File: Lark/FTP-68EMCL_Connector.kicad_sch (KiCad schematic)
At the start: 6 parts, among them J3 B34B-PHDSS

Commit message: added power section to schematic
It needs revised, due to thermal issue. Specifically in regards to my soft start circuit, the mosfet wont be able to handle the power dissipated during a slow turn on.
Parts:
- C16: value 0.1 µF -> 0.1µF
- C17: value 6800 µF -> 6800µF
- D7: footprint onsemi:D_SOD-523 -> onsemi:ESD5Z3.3T1G
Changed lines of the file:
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@@
 			)
 		)
-		(property "Datasheet" "https://www.seielect.com/catalog/SEI-RMCF_RMCP.pdf"
+		(property "Datasheet" "~"
 			(at 49.53 128.27 0)
 			(effects
@@
 			)
 		)
-		(property "Value" "0.1 µF"
+		(property "Value" "0.1µF"
 			(at 38.1 137.1662 0)
 			(effects
@@
 			)
 		)
-		(property "Datasheet" "https://search.murata.co.jp/Ceramy/image/img/A01X/G101/ENG/GRM188R72A104MA35-01A.pdf"
+		(property "Datasheet" "~"
 			(at 35.56 135.89 0)
 			(effects
@@
 			)
 		)
-		(property "Datasheet" "https://www.seielect.com/catalog/SEI-RMCF_RMCP.pdf"
+		(property "Datasheet" "~"
 			(at 35.56 119.38 0)
 			(effects
@@
 			)
 		)
-		(property "Value" "6800 µF"
+		(property "Value" "6800µF"
 			(at 92.71 128.6509 0)
 			(effects
@@
 			)
 		)
-		(property "Footprint" "onsemi:D_SOD-523"
+		(property "Footprint" "onsemi:ESD5Z3.3T1G"
 			(at 57.15 137.16 0)
 			(effects

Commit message: update, WIP
- Reannotated schematic.
- Added STM32 device.
- Fixed High-side switch (removed soft-start cap for device safety).
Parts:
- renumbered C17 to C26, C16 to C27, D7 to D9, J3 to J4, R34 to R41, R33 to R42
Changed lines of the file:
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@@
 		(on_board yes)
 		(dnp no)
-		(property "Reference" "R33"
+		(property "Reference" "R42"
 			(at 50.546 125.73 90)
 			(effects
@@
 			(project "Lark"
 				(path "/a351af57-4353-47da-9f45-7393de572768/6e291d34-e508-4d3b-a2e9-20acfef2b928"
-					(reference "R33")
+					(reference "R42")
 					(unit 1)
 				)
@@
 		(dnp no)
 		(fields_autoplaced yes)
-		(property "Reference" "#PWR069"
+		(property "Reference" "#PWR0109"
 			(at 226.06 33.02 0)
 			(effects
@@
 			(project "Lark"
 				(path "/a351af57-4353-47da-9f45-7393de572768/6e291d34-e508-4d3b-a2e9-20acfef2b928"
-					(reference "#PWR069")
+					(reference "#PWR0109")
 					(unit 1)
 				)
@@
 		(on_board yes)
 		(dnp no)
-		(property "Reference" "C16"
+		(property "Reference" "C27"
 			(at 38.1 134.6262 0)
 			(effects
@@
 			(project "Lark"
 				(path "/a351af57-4353-47da-9f45-7393de572768/6e291d34-e508-4d3b-a2e9-20acfef2b928"
-					(reference "C16")
+					(reference "C27")
 					(unit 1)
 				)
@@
 		(dnp no)
 		(fields_autoplaced yes)
-		(property "Reference" "#PWR088"
+		(property "Reference" "#PWR0110"
 			(at 251.46 33.02 0)
 			(effects
@@
 			(project "Lark"
 				(path "/a351af57-4353-47da-9f45-7393de572768/6e291d34-e508-4d3b-a2e9-20acfef2b928"
-					(reference "#PWR088")
+					(reference "#PWR0110")
 					(unit 1)
 				)
@@
 		(on_board yes)
 		(dnp no)
-		(property "Reference" "R34"
+		(property "Reference" "R41"
 			(at 38.1 118.1099 0)
 			(effects
@@
 			(project "Lark"
 				(path "/a351af57-4353-47da-9f45-7393de572768/6e291d34-e508-4d3b-a2e9-20acfef2b928"
-					(reference "R34")
+					(reference "R41")
 					(unit 1)
 				)
@@
 		(dnp no)
 		(fields_autoplaced yes)
-		(property "Reference" "#PWR090"
+		(property "Reference" "#PWR0114"
 			(at 248.92 95.25 0)
 			(effects
@@
 			(project "Lark"
 				(path "/a351af57-4353-47da-9f45-7393de572768/6e291d34-e508-4d3b-a2e9-20acfef2b928"
-					(reference "#PWR090")
+					(reference "#PWR0114")
 					(unit 1)
 				)
@@
 		(dnp no)
 		(fields_autoplaced yes)
-		(property "Reference" "#PWR071"
+		(property "Reference" "#PWR0113"
 			(at 228.6 95.25 0)
 			(effects
@@
 			(project "Lark"
 				(path "/a351af57-4353-47da-9f45-7393de572768/6e291d34-e508-4d3b-a2e9-20acfef2b928"
-					(reference "#PWR071")
+					(reference "#PWR0113")
 					(unit 1)
 				)
@@
 		(dnp no)
 		(fields_autoplaced yes)
-		(property "Reference" "#PWR091"
+		(property "Reference" "#PWR0116"
 			(at 88.9 115.57 0)
 			(effects
@@
 			(project "Lark"
 				(path "/a351af57-4353-47da-9f45-7393de572768/6e291d34-e508-4d3b-a2e9-20acfef2b928"
-					(reference "#PWR091")
+					(reference "#PWR0116")
 					(unit 1)
 				)
@@
 		(dnp no)
 		(fields_autoplaced yes)
-		(property "Reference" "#PWR070"
+		(property "Reference" "#PWR0111"
 			(at 220.98 39.37 0)
 			(effects
@@
 			(project "Lark"
 				(path "/a351af57-4353-47da-9f45-7393de572768/6e291d34-e508-4d3b-a2e9-20acfef2b928"
-					(reference "#PWR070")
+					(reference "#PWR0111")
 					(unit 1)
 				)
@@
 		(dnp no)
 		(fields_autoplaced yes)
-		(property "Reference" "#PWR086"
+		(property "Reference" "#PWR0115"
 			(at 35.56 115.57 0)
 			(effects
@@
 			(project "Lark"
 				(path "/a351af57-4353-47da-9f45-7393de572768/6e291d34-e508-4d3b-a2e9-20acfef2b928"
-					(reference "#PWR086")
+					(reference "#PWR0115")
 					(unit 1)
 				)
@@
 		(dnp no)
 		(fields_autoplaced yes)
-		(property "Reference" "C17"
+		(property "Reference" "C26"
 			(at 92.71 126.1109 0)
 			(effects
@@
 			(project ""
 				(path "/a351af57-4353-47da-9f45-7393de572768/6e291d34-e508-4d3b-a2e9-20acfef2b928"
-					(reference "C17")
+					(reference "C26")
 					(unit 1)
 				)
@@
 		(dnp no)
 		(fields_autoplaced yes)
-		(property "Reference" "D7"
+		(property "Reference" "D9"
 			(at 59.69 136.6201 90)
 			(effects
@@
 			(project "Lark"
 				(path "/a351af57-4353-47da-9f45-7393de572768/6e291d34-e508-4d3b-a2e9-20acfef2b928"
-					(reference "D7")
+					(reference "D9")
 					(unit 1)
 				)
@@
 		(dnp no)
 		(fields_autoplaced yes)
-		(property "Reference" "#PWR089"
+		(property "Reference" "#PWR0112"
 			(at 256.54 39.37 0)
 			(effects
@@
 			(project "Lark"
 				(path "/a351af57-4353-47da-9f45-7393de572768/6e291d34-e508-4d3b-a2e9-20acfef2b928"
-					(reference "#PWR089")
+					(reference "#PWR0112")
 					(unit 1)
 				)
@@
 		(on_board yes)
 		(dnp no)
-		(property "Reference" "J3"
+		(property "Reference" "J4"
 			(at 236.982 37.592 0)
 			(effects
@@
 			(project ""
 				(path "/a351af57-4353-47da-9f45-7393de572768/6e291d34-e508-4d3b-a2e9-20acfef2b928"
-					(reference "J3")
+					(reference "J4")
 					(unit 1)
 				)
@@
 		(dnp no)
 		(fields_autoplaced yes)
-		(property "Reference" "#PWR085"
+		(property "Reference" "#PWR0118"
 			(at 57.15 151.13 0)
 			(effects
@@
 			(project "Lark"
 				(path "/a351af57-4353-47da-9f45-7393de572768/6e291d34-e508-4d3b-a2e9-20acfef2b928"
-					(reference "#PWR085")
+					(reference "#PWR0118")
 					(unit 1)
 				)
@@
 		(dnp no)
 		(fields_autoplaced yes)
-		(property "Reference" "#PWR087"
+		(property "Reference" "#PWR0117"
 			(at 35.56 151.13 0)
 			(effects
@@
 			(project "Lark"
 				(path "/a351af57-4353-47da-9f45-7393de572768/6e291d34-e508-4d3b-a2e9-20acfef2b928"
-					(reference "#PWR087")
+					(reference "#PWR0117")
 					(unit 1)
 				)
@@
 		(dnp no)
 		(fields_autoplaced yes)
-		(property "Reference" "#PWR092"
+		(property "Reference" "#PWR0119"
 			(at 88.9 151.13 0)
 			(effects
@@
 			(project "Lark"
 				(path "/a351af57-4353-47da-9f45-7393de572768/6e291d34-e508-4d3b-a2e9-20acfef2b928"
-					(reference "#PWR092")
-					(unit 1)
-				)
+					(reference "#PWR0119")
+					(unit 1)
+				)

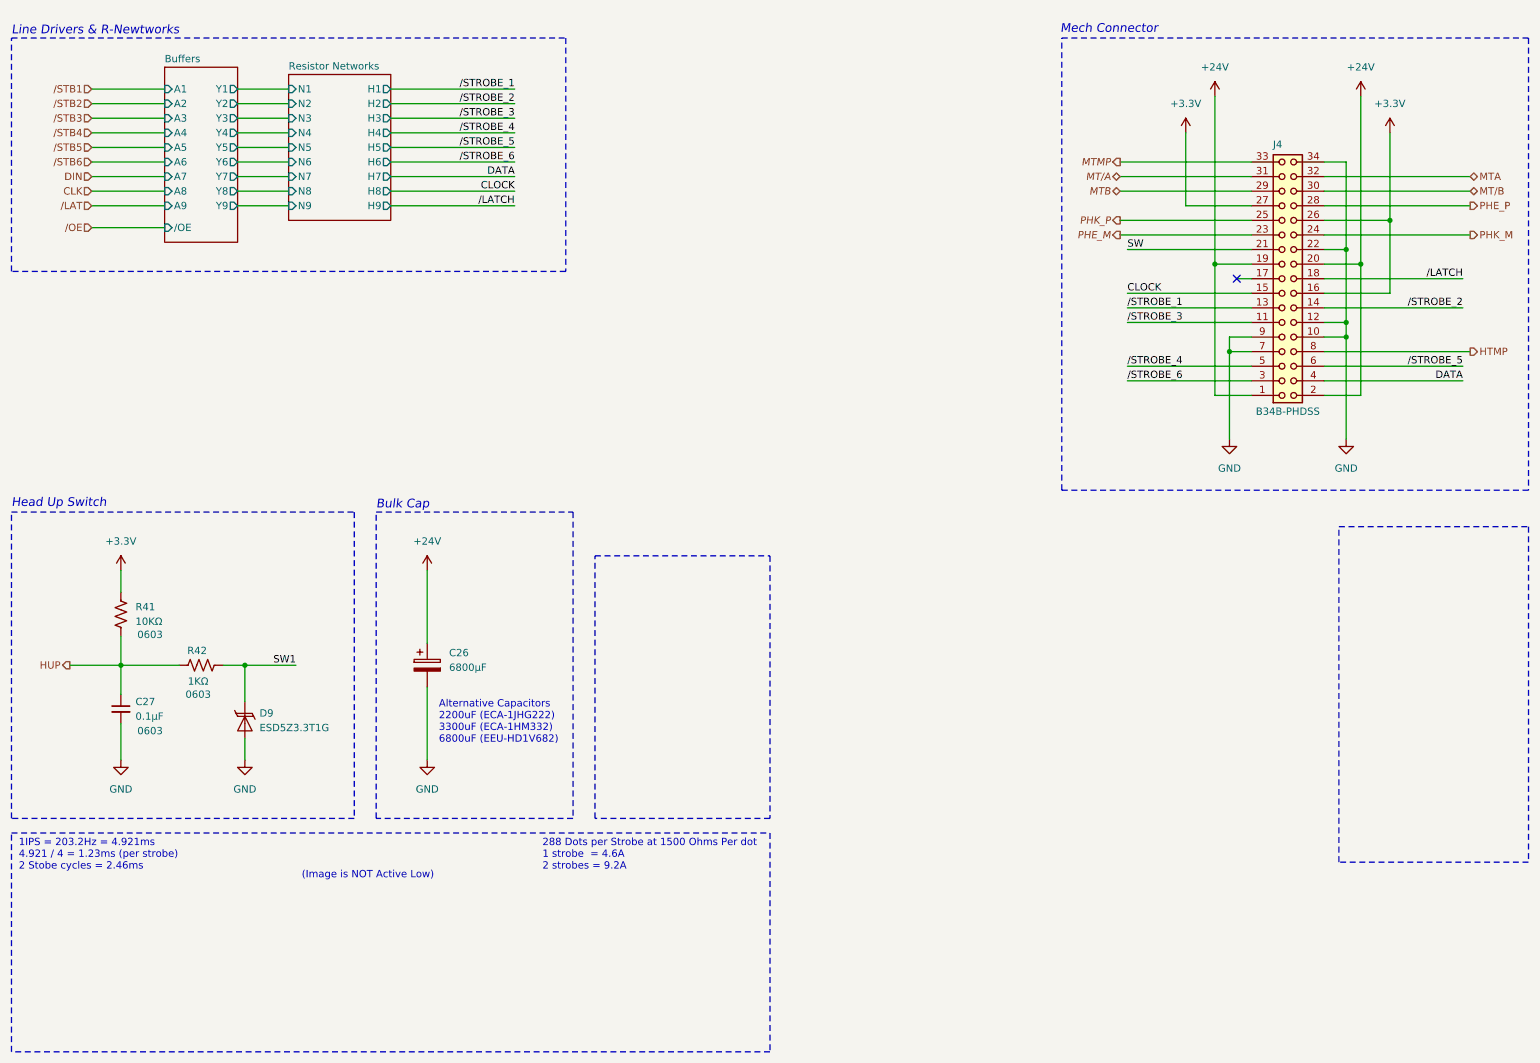
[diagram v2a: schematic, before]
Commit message: Updated schematic, WIP
- Added NOR flash part.
- Added new CubeMX config file.
- Reannotated the schematic.
- Made some more connections to the MCU.
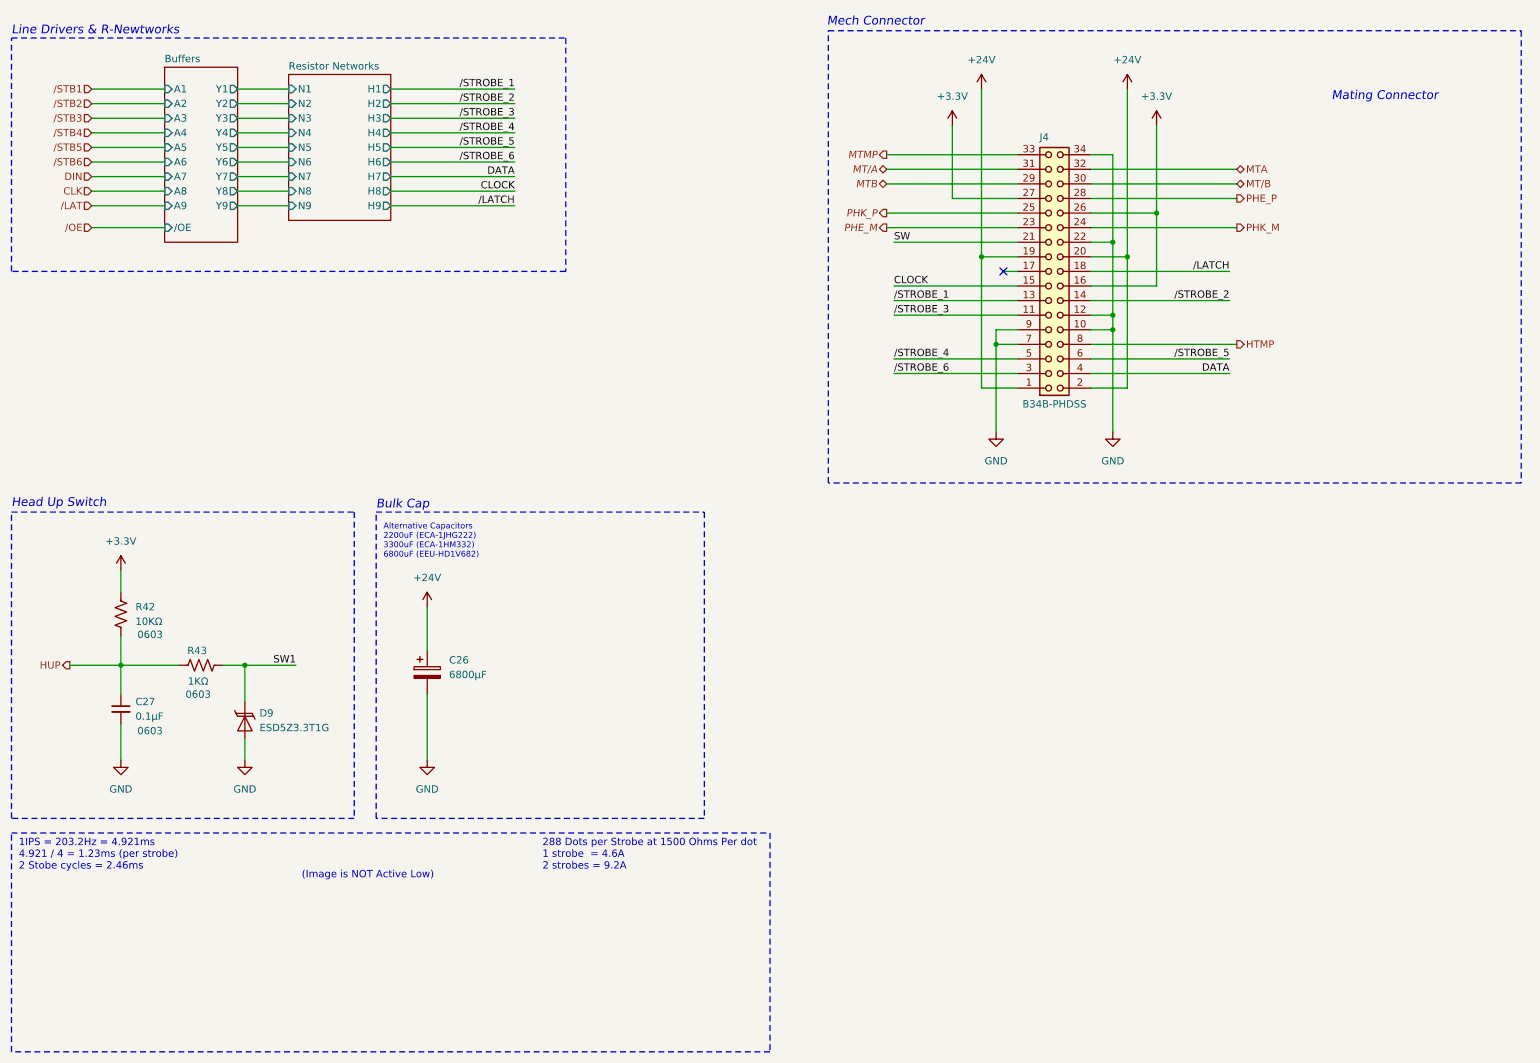
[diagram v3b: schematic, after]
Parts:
- renumbered R41 to R42, R42 to R43
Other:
- note added: "Mating Connector"
- moved on the sheet: C26, J4

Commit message: Update, WIP
- Added TVS diode to 24v Supply.
- Fixed bleeder circuit at some point (I think it was this commit)
- Added Jumper to connect NTC to ADC. (again I think it was this commit)
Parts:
- renumbered D9 to D10, R42 to R45, R43 to R46
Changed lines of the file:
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@@
 		(on_board yes)
 		(dnp no)
-		(property "Reference" "R43"
+		(property "Reference" "R46"
 			(at 50.546 125.73 90)
 			(effects
@@
 			(project "Lark"
 				(path "/a351af57-4353-47da-9f45-7393de572768/6e291d34-e508-4d3b-a2e9-20acfef2b928"
-					(reference "R43")
+					(reference "R46")
 					(unit 1)
 				)
@@
 		(dnp no)
 		(fields_autoplaced yes)
-		(property "Reference" "#PWR0109"
+		(property "Reference" "#PWR0113"
 			(at 185.42 31.75 0)
 			(effects
@@
 			(project "Lark"
 				(path "/a351af57-4353-47da-9f45-7393de572768/6e291d34-e508-4d3b-a2e9-20acfef2b928"
-					(reference "#PWR0109")
+					(reference "#PWR0113")
 					(unit 1)
 				)
@@
 		(dnp no)
 		(fields_autoplaced yes)
-		(property "Reference" "#PWR0110"
+		(property "Reference" "#PWR0114"
 			(at 210.82 31.75 0)
 			(effects
@@
 			(project "Lark"
 				(path "/a351af57-4353-47da-9f45-7393de572768/6e291d34-e508-4d3b-a2e9-20acfef2b928"
-					(reference "#PWR0110")
+					(reference "#PWR0114")
 					(unit 1)
 				)
@@
 		(on_board yes)
 		(dnp no)
-		(property "Reference" "R42"
+		(property "Reference" "R45"
 			(at 38.1 118.1099 0)
 			(effects
@@
 			(project "Lark"
 				(path "/a351af57-4353-47da-9f45-7393de572768/6e291d34-e508-4d3b-a2e9-20acfef2b928"
-					(reference "R42")
+					(reference "R45")
 					(unit 1)
 				)
@@
 		(dnp no)
 		(fields_autoplaced yes)
-		(property "Reference" "#PWR0114"
+		(property "Reference" "#PWR0118"
 			(at 208.28 93.98 0)
 			(effects
@@
 			(project "Lark"
 				(path "/a351af57-4353-47da-9f45-7393de572768/6e291d34-e508-4d3b-a2e9-20acfef2b928"
-					(reference "#PWR0114")
+					(reference "#PWR0118")
 					(unit 1)
 				)
@@
 		(dnp no)
 		(fields_autoplaced yes)
-		(property "Reference" "#PWR0113"
+		(property "Reference" "#PWR0117"
 			(at 187.96 93.98 0)
 			(effects
@@
 			(project "Lark"
 				(path "/a351af57-4353-47da-9f45-7393de572768/6e291d34-e508-4d3b-a2e9-20acfef2b928"
-					(reference "#PWR0113")
+					(reference "#PWR0117")
 					(unit 1)
 				)
@@
 		(dnp no)
 		(fields_autoplaced yes)
-		(property "Reference" "#PWR0116"
+		(property "Reference" "#PWR0120"
 			(at 88.9 121.92 0)
 			(effects
@@
 			(project "Lark"
 				(path "/a351af57-4353-47da-9f45-7393de572768/6e291d34-e508-4d3b-a2e9-20acfef2b928"
-					(reference "#PWR0116")
+					(reference "#PWR0120")
+					(unit 1)
+				)
+			)
+		)
+	)
+	(symbol
+		(lib_id "JST Sales America Inc:B34B-PHDSS")
+		(at 196.85 59.69 0)
+		(mirror x)
+		(unit 1)
+		(exclude_from_sim no)
+		(in_bom yes)
+		(on_board yes)
+		(dnp no)
+		(property "Reference" "J4"
+			(at 196.342 36.322 0)
+			(effects
+				(font
+					(size 1.27 1.27)
+				)
+			)
+		)
+		(property "Value" "B34B-PHDSS"
+			(at 198.12 82.804 0)
+			(effects
+				(font
+					(size 1.27 1.27)
+				)
+			)
+		)
+		(property "Footprint" "JST Sales America Inc:JST_PHD_B34B-PHDSS_2x17_P2.00mm_Vertical"
+			(at 197.358 28.448 0)
+			(effects
+				(font
+					(size 1.27 1.27)
+				)
+				(hide yes)
+			)
+		)
+		(property "Datasheet" "https://www.jst-mfg.com/product/pdf/eng/ePHD.pdf"
+			(at 197.612 30.988 0)
+			(effects
+				(font
+					(size 1.27 1.27)
+				)
+				(hide yes)
+			)
+		)
+		(property "Description" "Connector Header Through Hole 34 position 0.079\" (2.00mm)"
+			(at 198.628 33.274 0)
+			(effects
+				(font
+					(size 1.27 1.27)
+				)
+				(hide yes)
+			)
+		)
+		(property "MPN" "B34B-PHDSS"
+			(at 198.628 36.83 0)
+			(effects
+				(font
+					(size 1.27 1.27)
+				)
+				(hide yes)
+			)
+		)
+		(pin "7"
+		)
+		(pin "11"
+		)
+		(pin "21"
+		)
+		(pin "5"
+		)
+		(pin "3"
+		)
+		(pin "13"
+		)
+		(pin "23"
+		)
+		(pin "27"
+		)
+		(pin "1"
+		)
+		(pin "9"
+		)
+		(pin "17"
+		)
+		(pin "15"
+		)
+		(pin "19"
+		)
+		(pin "25"
+		)
+		(pin "29"
+		)
+		(pin "31"
+		)
+		(pin "33"
+		)
+		(pin "2"
+		)
+		(pin "10"
+		)
+		(pin "4"
+		)
+		(pin "8"
+		)
+		(pin "6"
+		)
+		(pin "12"
+		)
+		(pin "16"
+		)
+		(pin "22"
+		)
+		(pin "24"
+		)
+		(pin "26"
+		)
+		(pin "28"
+		)
+		(pin "30"
+		)
+		(pin "18"
+		)
+		(pin "20"
+		)
+		(pin "34"
+		)
+		(pin "14"
+		)
+		(pin "32"
+		)
+		(instances
+			(project "Lark"
+				(path "/a351af57-4353-47da-9f45-7393de572768/6e291d34-e508-4d3b-a2e9-20acfef2b928"
+					(reference "J4")
 					(unit 1)
 				)
@@
 		(dnp no)
 		(fields_autoplaced yes)
-		(property "Reference" "#PWR0111"
+		(property "Reference" "#PWR0115"
 			(at 180.34 38.1 0)
 			(effects
@@
 			(project "Lark"
 				(path "/a351af57-4353-47da-9f45-7393de572768/6e291d34-e508-4d3b-a2e9-20acfef2b928"
-					(reference "#PWR0111")
+					(reference "#PWR0115")
 					(unit 1)
 				)
@@
 		(dnp no)
 		(fields_autoplaced yes)
-		(property "Reference" "#PWR0115"
+		(property "Reference" "#PWR0119"
 			(at 35.56 115.57 0)
 			(effects
@@
 			(project "Lark"
 				(path "/a351af57-4353-47da-9f45-7393de572768/6e291d34-e508-4d3b-a2e9-20acfef2b928"
-					(reference "#PWR0115")
+					(reference "#PWR0119")
 					(unit 1)
 				)
@@
 		(dnp no)
 		(fields_autoplaced yes)
-		(property "Reference" "D9"
+		(property "Reference" "D10"
 			(at 59.69 136.6201 90)
 			(effects
@@
 			(project "Lark"
 				(path "/a351af57-4353-47da-9f45-7393de572768/6e291d34-e508-4d3b-a2e9-20acfef2b928"
-					(reference "D9")
+					(reference "D10")
 					(unit 1)
 				)
@@
 		(dnp no)
 		(fields_autoplaced yes)
-		(property "Reference" "#PWR0112"
+		(property "Reference" "#PWR0116"
 			(at 215.9 38.1 0)
 			(effects
@@
 			(project "Lark"
 				(path "/a351af57-4353-47da-9f45-7393de572768/6e291d34-e508-4d3b-a2e9-20acfef2b928"
-					(reference "#PWR0112")
-					(unit 1)
-				)
-			)
-		)
-	)
-	(symbol
-		(lib_id "JST Sales America Inc:B34B-PHDSS")
-		(at 196.85 59.69 0)
-		(mirror x)
-		(unit 1)
-		(exclude_from_sim no)
-		(in_bom yes)
-		(on_board yes)
-		(dnp no)
-		(property "Reference" "J4"
-			(at 196.342 36.322 0)
-			(effects
-				(font
-					(size 1.27 1.27)
-				)
-			)
-		)
-		(property "Value" "B34B-PHDSS"
-			(at 198.12 82.804 0)
-			(effects
-				(font
-					(size 1.27 1.27)
-				)
-			)
-		)
-		(property "Footprint" "JST Sales America Inc:JST_PHD_B34B-PHDSS_2x17_P2.00mm_Vertical"
-			(at 197.358 28.448 0)
-			(effects
-				(font
-					(size 1.27 1.27)
-				)
-				(hide yes)
-			)
-		)
-		(property "Datasheet" "https://www.jst-mfg.com/product/pdf/eng/ePHD.pdf"
-			(at 197.612 30.988 0)
-			(effects
-				(font
-					(size 1.27 1.27)
-				)
-				(hide yes)
-			)
-		)
-		(property "Description" "Connector Header Through Hole 34 position 0.079\" (2.00mm)"
-			(at 198.628 33.274 0)
-			(effects
-				(font
-					(size 1.27 1.27)
-				)
-				(hide yes)
-			)
-		)
-		(property "MPN" "B34B-PHDSS"
-			(at 198.628 36.83 0)
-			(effects
-				(font
-					(size 1.27 1.27)
-				)
-				(hide yes)
-			)
-		)
-		(pin "7"
-		)
-		(pin "11"
-		)
-		(pin "21"
-		)
-		(pin "5"
-		)
-		(pin "3"
-		)
-		(pin "13"
-		)
-		(pin "23"
-		)
-		(pin "27"
-		)
-		(pin "1"
-		)
-		(pin "9"
-		)
-		(pin "17"
-		)
-		(pin "15"
-		)
-		(pin "19"
-		)
-		(pin "25"
-		)
-		(pin "29"
-		)
-		(pin "31"
-		)
-		(pin "33"
-		)
-		(pin "2"
-		)
-		(pin "10"
-		)
-		(pin "4"
-		)
-		(pin "8"
-		)
-		(pin "6"
-		)
-		(pin "12"
-		)
-		(pin "16"
-		)
-		(pin "22"
-		)
-		(pin "24"
-		)
-		(pin "26"
-		)
-		(pin "28"
-		)
-		(pin "30"
-		)
-		(pin "18"
-		)
-		(pin "20"
-		)
-		(pin "34"
-		)
-		(pin "14"
-		)
-		(pin "32"
-		)
-		(instances
-			(project ""
-				(path "/a351af57-4353-47da-9f45-7393de572768/6e291d34-e508-4d3b-a2e9-20acfef2b928"
-					(reference "J4")
+					(reference "#PWR0116")
 					(unit 1)
 				)
@@
 		(dnp no)
 		(fields_autoplaced yes)
-		(property "Reference" "#PWR0118"
+		(property "Reference" "#PWR0122"
 			(at 57.15 151.13 0)
 			(effects
@@
 			(project "Lark"
 				(path "/a351af57-4353-47da-9f45-7393de572768/6e291d34-e508-4d3b-a2e9-20acfef2b928"
-					(reference "#PWR0118")
+					(reference "#PWR0122")
 					(unit 1)
 				)
@@
 		(dnp no)
 		(fields_autoplaced yes)
-		(property "Reference" "#PWR0117"
+		(property "Reference" "#PWR0121"
 			(at 35.56 151.13 0)
 			(effects
@@
 			(project "Lark"
 				(path "/a351af57-4353-47da-9f45-7393de572768/6e291d34-e508-4d3b-a2e9-20acfef2b928"
-					(reference "#PWR0117")
+					(reference "#PWR0121")
 					(unit 1)
 				)
@@
 		(dnp no)
 		(fields_autoplaced yes)
-		(property "Reference" "#PWR0119"
+		(property "Reference" "#PWR0123"
 			(at 88.9 151.13 0)
 			(effects
@@
 			(project "Lark"
 				(path "/a351af57-4353-47da-9f45-7393de572768/6e291d34-e508-4d3b-a2e9-20acfef2b928"
-					(reference "#PWR0119")
-					(unit 1)
-				)
+					(reference "#PWR0123")
+					(unit 1)
+				)
